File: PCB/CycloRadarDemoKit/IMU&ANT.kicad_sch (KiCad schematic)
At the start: 0 parts

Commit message: MPU added, power managemennt updated
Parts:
- added C501: 10nF/10V(10%), symbol Device:C_Small
- added C502: 0.1uF/10V(10%), symbol Device:C_Small
- added C503, C504: 100nF/10V, symbol Device:C_Small
- added C505: 0.1uF/2V(10%), symbol Device:C_Small
- added C506: 2.2nF/50V(10%), symbol Device:C_Small
- added R501, R502: 0R, symbol Device:R
- added U302: D52MxxM8, RF_Module:Garmin_M8-35_9.8x14.0mm_Layout6x6_P1.5mm, symbol RF_Module:D52MxxM8
- added U501: MPU-6050, Sensor_Motion:InvenSense_QFN-24_4x4mm_P0.5mm, symbol Sensor_Motion:MPU-6050
- added U502: LSM6DSM, Package_LGA:LGA-14_3x2.5mm_P0.5mm_LayoutBorder3x4y, symbol Sensor_Motion:LSM6DSM
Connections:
- new net: U302.A2 (VSS), U302.A3 (VSS), U302.A4 (VSS), U302.A5 (VSS), U302.A6 (VSS)
- new net: U302.B5 (VCC), U302.B6 (VCC), U302.C5 (VCC), U302.C6 (VCC)
- new net: C505.1, U501.10 (REGOUT)
- new net: C501.1, C502.1, R501.2, U501.13 (VDD), U501.8 (VLOGIC)
- new net: C503.1, C504.1, R502.2, U502.12 (CS), U502.5 (VDDIO), U502.8 (VDD)
- new net: C506.1, U501.20 (CPOUT)
- new net +3V3: R501.1, R502.1
- new net GND: C501.2, C502.2, C503.2, C504.2, C505.2, C506.2, U501.1 (CLKIN), U501.11 (FSYNC), U501.18 (GND), U501.9 (AD0), U502.1 (SDO/SA0), U502.2 (SDX), U502.3 (SCX), U502.6 (GND), U502.7 (GND)
- new net IMU_INT: U501.12 (INT), U502.4 (INT1)
- new net SCL: U501.23 (SCL), U502.13 (SCL)
- new net SDA: U501.24 (SDA), U502.14 (SDA)
- no-connect marks 0 -> 5
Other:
- note added: "LSM I2C addr.: 0b1101010"
- note added: "MPU I2C addr.: 0b1101000"

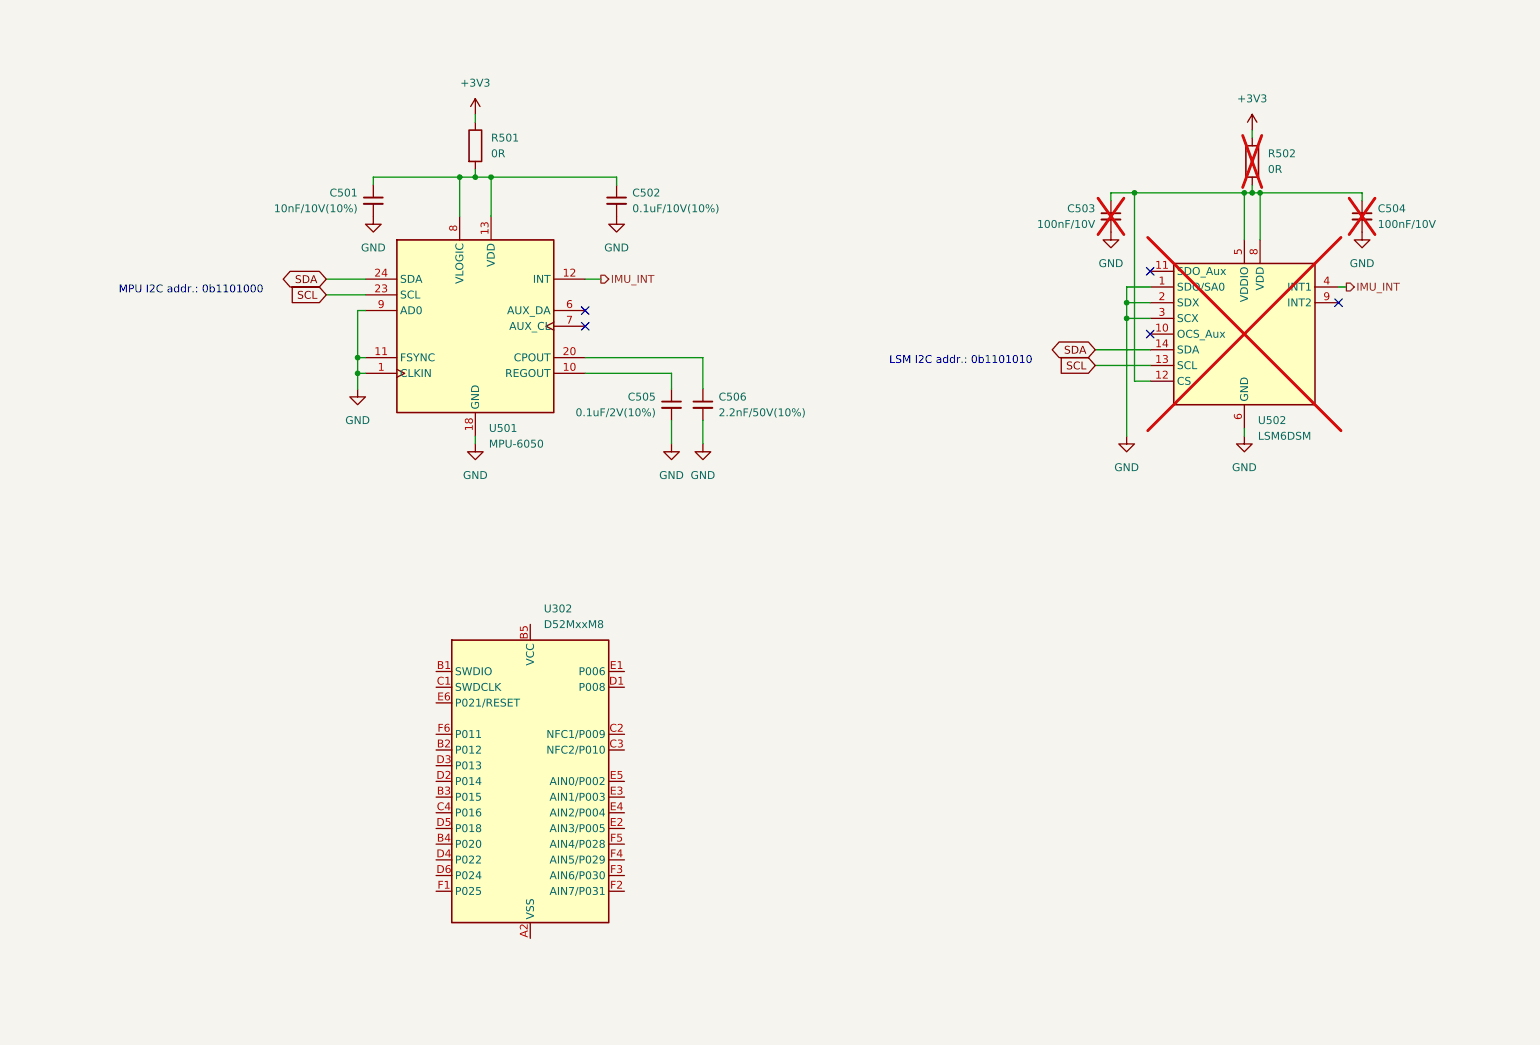
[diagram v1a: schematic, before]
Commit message: added buzzer and pins for Radar
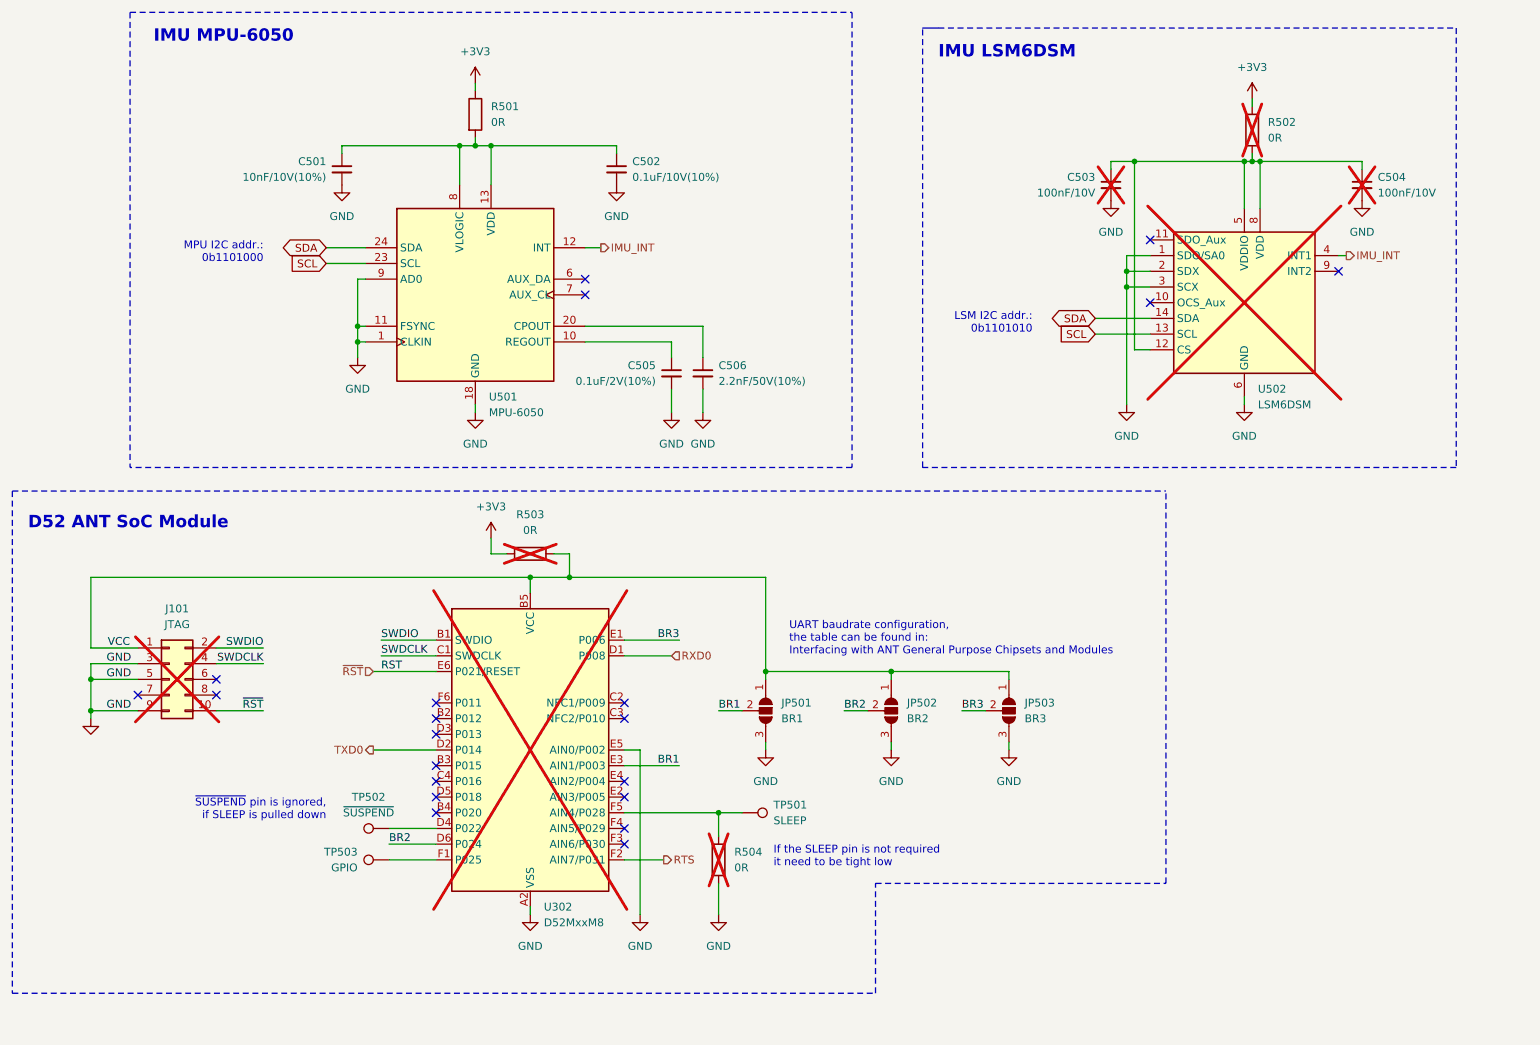
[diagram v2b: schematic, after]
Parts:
- added J101: JTAG, Connector_PinHeader_1.27mm:PinHeader_2x05_P1.27mm_Vertical_SMD, symbol Connector_Generic:Conn_02x05_Odd_Even
- added JP501: BR1, Jumper:SolderJumper-3_P1.3mm_Open_RoundedPad1.0x1.5mm_NumberLabels, symbol Jumper:SolderJumper_3_Open
- added JP502: BR2, Jumper:SolderJumper-3_P1.3mm_Open_RoundedPad1.0x1.5mm_NumberLabels, symbol Jumper:SolderJumper_3_Open
- added JP503: BR3, Jumper:SolderJumper-3_P1.3mm_Open_RoundedPad1.0x1.5mm_NumberLabels, symbol Jumper:SolderJumper_3_Open
- added R503, R504: 0R, Resistor_SMD:R_0603_1608Metric, symbol Device:R
- added TP501: SLEEP, symbol Connector:TestPoint
- added TP502: ~{SUSPEND}, symbol Connector:TestPoint
- added TP503: GPIO, symbol Connector:TestPoint
- C503, C504: footprint (none) -> Capacitor_SMD:C_0603_1608Metric
- R502: footprint (none) -> Resistor_SMD:R_0603_1608Metric
- U302: now not fitted
- U501: LCSC (none) -> C24112
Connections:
- net +3V3: now also R503.1
- net GND: now also U302.A2 (VSS), U302.A3 (VSS), U302.A4 (VSS), U302.A5 (VSS), U302.A6 (VSS), U302.E5 (AIN0/P002), J101.3 (Pin_3), J101.5 (Pin_5), J101.9 (Pin_9), JP501.3 (B), JP502.3 (B), JP503.3 (B), R504.2
- net SWDIO: now reaches U302.B1 (SWDIO)
- net SWDIO: now also J101.2 (Pin_2)
- net VCC: now reaches U302.B5 (VCC), U302.B6 (VCC), U302.C5 (VCC), U302.C6 (VCC)
- net VCC: now also J101.1 (Pin_1), JP501.1 (A), JP502.1 (A), JP503.1 (A), R503.2
- net SWDCLK: now reaches U302.C1 (SWDCLK)
- net SWDCLK: now also J101.4 (Pin_4)
- net RXD0: now reaches U302.D1 (P008)
- net TXD0: now reaches U302.D2 (P014)
- net at U302.D4 (P022): now also TP502.1
- net BR2: now reaches U302.D6 (P024)
- net BR2: now also JP502.2 (C)
- net BR3: now reaches U302.E1 (P006)
- net BR3: now also JP503.2 (C)
- net BR1: now reaches U302.E3 (AIN1/P003)
- net BR1: now also JP501.2 (C)
- net ~{RST}: now reaches U302.E6 (P021/RESET)
- net ~{RST}: now also J101.10 (Pin_10)
- net at U302.F1 (P025): now also TP503.1
- net RTS: now reaches U302.F2 (AIN7/P031)
- net at U302.F5 (AIN4/P028): now also R504.1, TP501.1
- no-connect marks 5 -> 21
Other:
- note added: "D52 ANT SoC Module"
- note added: "IMU LSM6DSM"
- note added: "IMU MPU-6050"
- note added: "If the SLEEP pin is not required it need to be tight low"
- note added: "UART baudrate configuration, the table can be found in: Interfacing with ANT General Purpose Chipsets and Modules"
- note added: "~{SUSPEND} pin is ignored, if SLEEP is pulled down"
- moved on the sheet: C501, C502, C503, C504, C505, C506, R501, R502, U501, U502

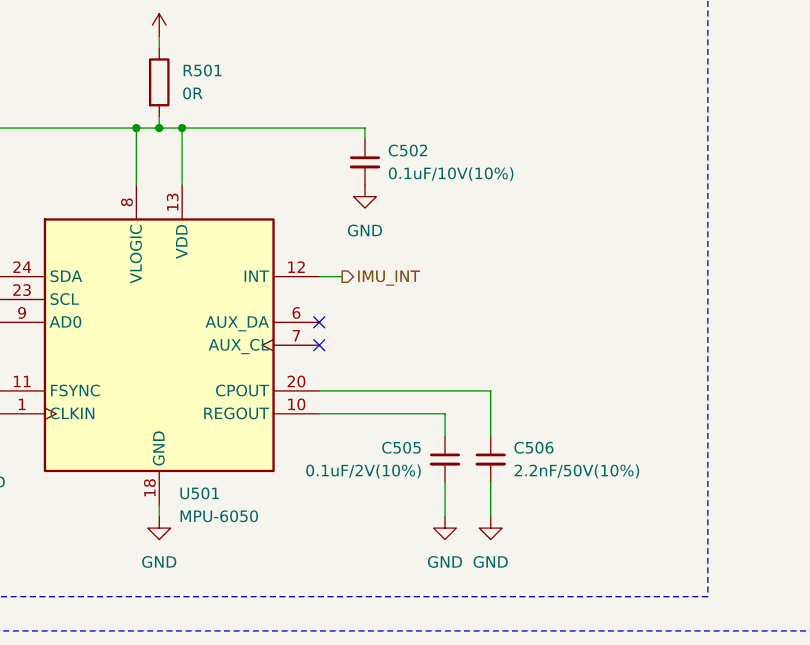
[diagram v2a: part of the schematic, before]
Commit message: more components fthprnt added
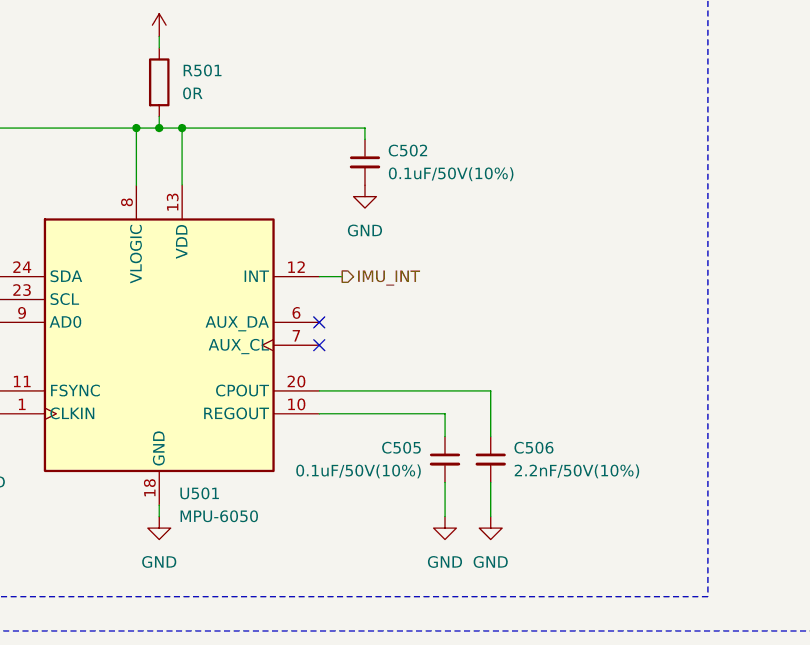
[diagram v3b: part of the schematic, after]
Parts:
- C502: value 0.1uF/10V(10%) -> 0.1uF/50V(10%); footprint (none) -> Capacitor_SMD:C_0603_1608Metric; LCSC (none) -> C14663
- C503, C504: footprint Capacitor_SMD:C_0603_1608Metric -> (none)
- C505: value 0.1uF/2V(10%) -> 0.1uF/50V(10%); footprint (none) -> Capacitor_SMD:C_0603_1608Metric; LCSC (none) -> C14663
- R501: footprint (none) -> Resistor_SMD:R_0805_2012Metric; LCSC (none) -> C17477
- R502, R503, R504: footprint Resistor_SMD:R_0603_1608Metric -> Resistor_SMD:R_0805_2012Metric; LCSC (none) -> C17477
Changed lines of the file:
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@@
       (effects (font (size 1.27 1.27)) (justify left))
     )
-    (property "Value" "0.1uF/2V(10%)" (at 129.54 80.0163 0)
-      (effects (font (size 1.27 1.27)) (justify left))
-    )
-    (property "Footprint" "" (at 132.08 78.74 0)
+    (property "Value" "0.1uF/50V(10%)" (at 129.54 80.0163 0)
+      (effects (font (size 1.27 1.27)) (justify left))
+    )
+    (property "Footprint" "Capacitor_SMD:C_0603_1608Metric" (at 132.08 78.74 0)
       (effects (font (size 1.27 1.27)) hide)
     )
@@
       (effects (font (size 1.27 1.27)) hide)
     )
+    (property "LCSC" "C14663" (at 132.08 78.74 0)
+      (effects (font (size 1.27 1.27)) hide)
+    )
     (pin "2")
     (pin "1")
@@
       (effects (font (size 1.27 1.27)) (justify left))
     )
-    (property "Footprint" "" (at 98.552 36.83 90)
+    (property "Footprint" "Resistor_SMD:R_0805_2012Metric" (at 98.552 36.83 90)
       (effects (font (size 1.27 1.27)) hide)
     )
     (property "Datasheet" "~" (at 100.33 36.83 0)
+      (effects (font (size 1.27 1.27)) hide)
+    )
+    (property "LCSC" "C17477" (at 100.33 36.83 0)
       (effects (font (size 1.27 1.27)) hide)
     )
@@
       (effects (font (size 1.27 1.27)) (justify left))
     )
-    (property "Value" "0.1uF/10V(10%)" (at 125.73 46.9963 0)
-      (effects (font (size 1.27 1.27)) (justify left))
-    )
-    (property "Footprint" "" (at 123.19 45.72 0)
+    (property "Value" "0.1uF/50V(10%)" (at 125.73 46.9963 0)
+      (effects (font (size 1.27 1.27)) (justify left))
+    )
+    (property "Footprint" "Capacitor_SMD:C_0603_1608Metric" (at 123.19 45.72 0)
       (effects (font (size 1.27 1.27)) hide)
     )
     (property "Datasheet" "~" (at 123.19 45.72 0)
+      (effects (font (size 1.27 1.27)) hide)
+    )
+    (property "LCSC" "C14663" (at 123.19 45.72 0)
       (effects (font (size 1.27 1.27)) hide)
     )
@@
       (effects (font (size 1.27 1.27)))
     )
-    (property "Footprint" "Resistor_SMD:R_0603_1608Metric" (at 109.22 109.728 90)
+    (property "Footprint" "Resistor_SMD:R_0805_2012Metric" (at 109.22 109.728 90)
       (effects (font (size 1.27 1.27)) hide)
     )
     (property "Datasheet" "~" (at 109.22 107.95 0)
+      (effects (font (size 1.27 1.27)) hide)
+    )
+    (property "LCSC" "C17477" (at 109.22 107.95 0)
       (effects (font (size 1.27 1.27)) hide)
     )
@@
       (effects (font (size 1.27 1.27)) (justify left))
     )
-    (property "Footprint" "Capacitor_SMD:C_0603_1608Metric" (at 243.84 48.26 0)
+    (property "Footprint" "" (at 243.84 48.26 0)
       (effects (font (size 1.27 1.27)) hide)
     )
@@
       (effects (font (size 1.27 1.27)) (justify left))
     )
-    (property "Footprint" "Resistor_SMD:R_0603_1608Metric" (at 137.922 157.48 90)
+    (property "Footprint" "Resistor_SMD:R_0805_2012Metric" (at 137.922 157.48 90)
       (effects (font (size 1.27 1.27)) hide)
     )
     (property "Datasheet" "~" (at 139.7 157.48 0)
+      (effects (font (size 1.27 1.27)) hide)
+    )
+    (property "LCSC" "C17477" (at 139.7 157.48 0)
       (effects (font (size 1.27 1.27)) hide)
     )
@@
       (effects (font (size 1.27 1.27)) (justify left))
     )
-    (property "Footprint" "Resistor_SMD:R_0603_1608Metric" (at 224.282 39.37 90)
+    (property "Footprint" "Resistor_SMD:R_0805_2012Metric" (at 224.282 39.37 90)
       (effects (font (size 1.27 1.27)) hide)
     )
     (property "Datasheet" "~" (at 226.06 39.37 0)
+      (effects (font (size 1.27 1.27)) hide)
+    )
+    (property "LCSC" "C17477" (at 226.06 39.37 0)
       (effects (font (size 1.27 1.27)) hide)
     )
@@
       (effects (font (size 1.27 1.27)) (justify left))
     )
-    (property "Footprint" "Capacitor_SMD:C_0603_1608Metric" (at 203.2 48.26 0)
-      (effects (font (size 1.27 1.27)) hide)
-    )
+    (property "Footprint" "" (at 203.2 48.26 0)
+      (effects (font (size 1.27 1.27)) hide)
+    )
